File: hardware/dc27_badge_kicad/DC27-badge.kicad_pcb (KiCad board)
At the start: 4 copper layers, 79.1 x 184.5 mm, 141 parts, among them J101 Conn_ARM_JTAG_SWD_10, J102 ShittyAddOnL, J103 ShittyAddOnR, J104 Conn_02x20_Odd_Even, J601 USB_MICRO_RIGHT, Q401 FDN360P, SW108 RESET, SW401 POWER ON, SW801 SKRHAAE010, SW802 SKRHAAE010, U100 BMD-340-A-R-DC27-peripheral-c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, U301 IS31FL3736-QFLS4-TR, U401 MCP73833, U402 LM1117-3.3, U501 CS4344-CZZ, U502 LM4880, U601 CP2102N-A01-GQFN28, U602 TPD3E001DRLR, Y101 32.768Khz XTAL

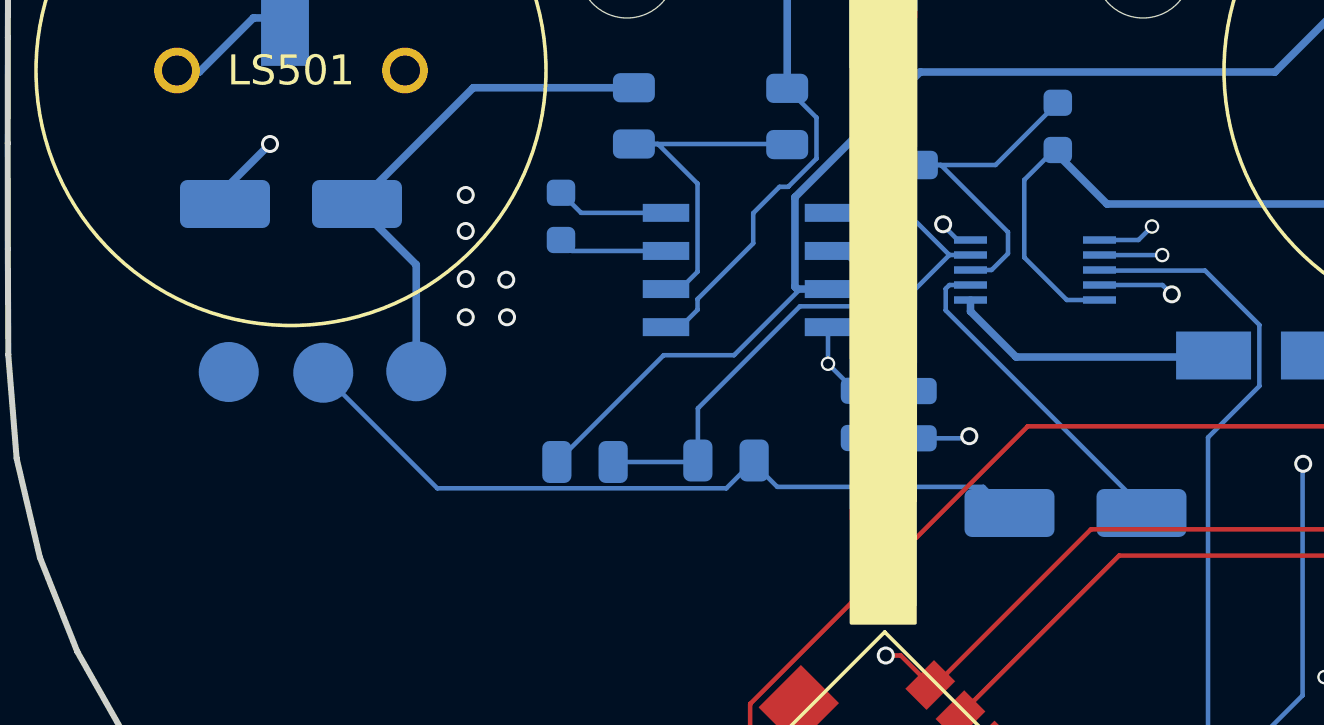
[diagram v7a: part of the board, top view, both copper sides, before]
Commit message: update schematic and pcb with proper audio cap polarity
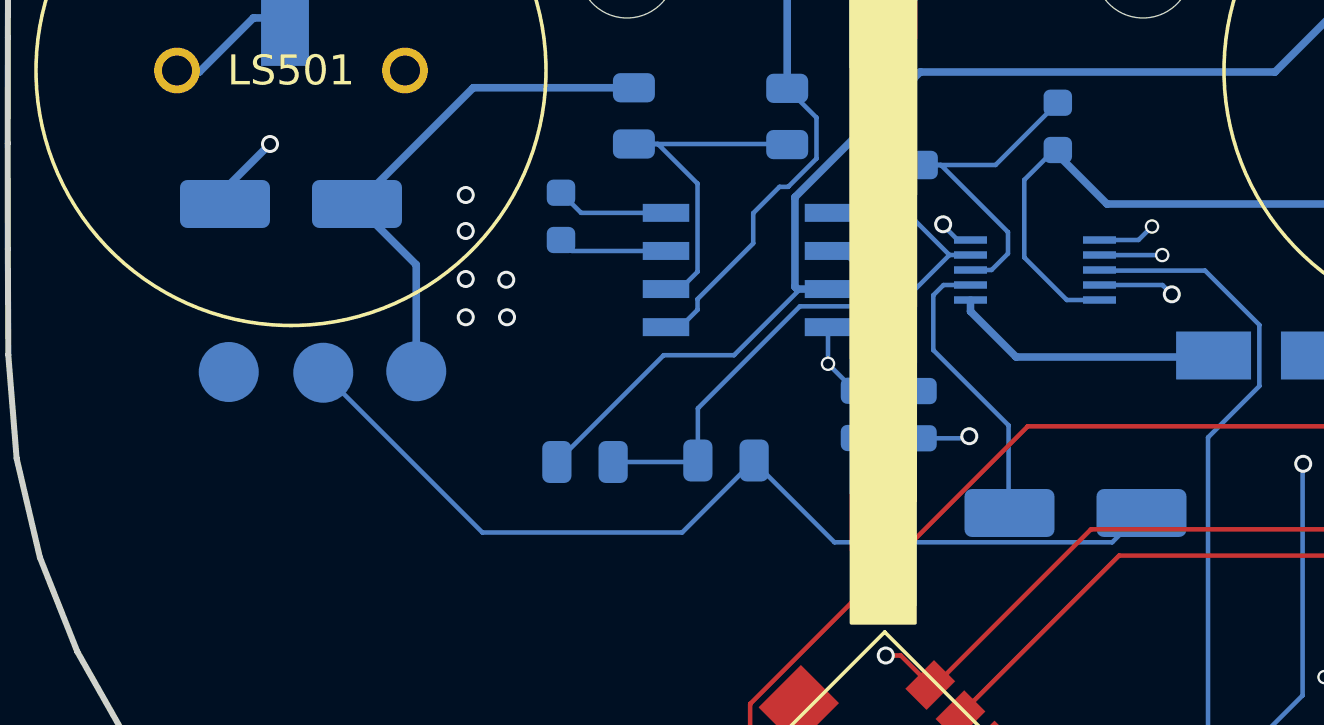
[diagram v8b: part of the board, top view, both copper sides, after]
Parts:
- turned C504 to 0 degrees
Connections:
- R502 pad 2: Net-(C504-Pad1) -> Net-(C504-Pad2)
- R503 pad 2: Net-(C506-Pad1) -> Net-(C506-Pad2)
- TP501 pad 1: Net-(C504-Pad1) -> Net-(C504-Pad2)
- TP502 pad 1: Net-(C506-Pad1) -> Net-(C506-Pad2)
- U501 pad 10: Net-(C504-Pad2) -> Net-(C504-Pad1)
- U501 pad 7: Net-(C506-Pad2) -> Net-(C506-Pad1)
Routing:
- net Net-(C506-Pad2): track 10.6 -> 32.0 mm
- net Net-(C506-Pad1): track 25.7 -> 9.58 mm
- net Net-(C504-Pad2): track 27.7 -> 17.0 mm, vias 2 -> 0
- net Net-(C504-Pad1): track 17.0 -> 27.7 mm, vias 0 -> 2
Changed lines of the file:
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@@
     (thickness 1.6)
     (drawings 191)
-    (tracks 2599)
+    (tracks 2601)
     (zones 0)
     (modules 141)
@@
     )
     (pad 1 smd circle (at 0 0) (size 2 2) (layers B.Cu B.Mask)
-      (net 61 "Net-(C506-Pad1)"))
+      (net 90 "Net-(C506-Pad2)"))
   )
   (module TestPoint:TestPoint_Pad_D2.0mm (layer B.Cu)
@@
     )
     (pad 1 smd circle (at 0 0) (size 2 2) (layers B.Cu B.Mask)
-      (net 53 "Net-(C504-Pad1)"))
+      (net 91 "Net-(C504-Pad2)"))
   )
   (module Diode_SMD:D_0805_2012Metric (layer F.Cu)
@@
   )
   (module Capacitor_SMD:CP_Elec_5x5.3 (layer B.Cu)
-    (at 85.4 53.2 180)
+    (at 85.4 53.2)
     (descr "SMD capacitor, aluminum electrolytic, Nichicon, 5.0x5.3mm")
     (tags "capacitor electrolytic")
     (attr smd)
-    (fp_text reference C504 (at 0 3.7 180) (layer B.SilkS)
+    (fp_text reference C504 (at 0 3.7) (layer B.SilkS)
       (effects (font (size 1 1) (thickness 0.15)) (justify mirror))
     )
-    (fp_text value 3.3uF (at 0 -3.7 180) (layer B.Fab)
+    (fp_text value 3.3uF (at 0 -3.7) (layer B.Fab)
       (effects (font (size 1 1) (thickness 0.15)) (justify mirror))
     )
-    (fp_text user %R (at 0 0 180) (layer B.Fab)
+    (fp_text user %R (at 0 0) (layer B.Fab)
       (effects (font (size 1 1) (thickness 0.15)) (justify mirror))
     )
@@
     (fp_line (start 2.65 2.65) (end 2.65 -2.65) (layer B.Fab) (width 0.1))
     (fp_circle (center 0 0) (end 2.5 0) (layer B.Fab) (width 0.1))
-    (pad 2 smd roundrect (at 2.2 0 180) (size 3 1.6) (layers B.Cu B.Paste B.Mask) (roundrect_rratio 0.15625)
+    (pad 2 smd roundrect (at 2.2 0) (size 3 1.6) (layers B.Cu B.Paste B.Mask) (roundrect_rratio 0.15625)
       (net 91 "Net-(C504-Pad2)"))
-    (pad 1 smd roundrect (at -2.2 0 180) (size 3 1.6) (layers B.Cu B.Paste B.Mask) (roundrect_rratio 0.15625)
+    (pad 1 smd roundrect (at -2.2 0) (size 3 1.6) (layers B.Cu B.Paste B.Mask) (roundrect_rratio 0.15625)
       (net 53 "Net-(C504-Pad1)"))
     (model ${KISYS3DMOD}/Capacitor_SMD.3dshapes/CP_Elec_5x5.3.wrl
@@
     (fp_line (start -1 -0.6) (end -1 0.6) (layer B.Fab) (width 0.1))
     (pad 2 smd roundrect (at 0.9375 0 90) (size 0.975 1.4) (layers B.Cu B.Paste B.Mask) (roundrect_rratio 0.25)
-      (net 53 "Net-(C504-Pad1)"))
+      (net 91 "Net-(C504-Pad2)"))
     (pad 1 smd roundrect (at -0.9375 0 90) (size 0.975 1.4) (layers B.Cu B.Paste B.Mask) (roundrect_rratio 0.25)
       (net 52 "Net-(R501-Pad2)"))
@@
     (fp_line (start -1 -0.6) (end -1 0.6) (layer B.Fab) (width 0.1))
     (pad 2 smd roundrect (at 0.9375 0) (size 0.975 1.4) (layers B.Cu B.Paste B.Mask) (roundrect_rratio 0.25)
-      (net 61 "Net-(C506-Pad1)"))
+      (net 90 "Net-(C506-Pad2)"))
     (pad 1 smd roundrect (at -0.9375 0) (size 0.975 1.4) (layers B.Cu B.Paste B.Mask) (roundrect_rratio 0.25)
       (net 62 "Net-(R503-Pad1)"))
@@
       (net 89 "Net-(C509-Pad1)"))
     (pad 7 smd rect (at 2.15 -0.5 180) (size 1.1 0.25) (layers B.Cu B.Paste B.Mask)
-      (net 90 "Net-(C506-Pad2)"))
+      (net 61 "Net-(C506-Pad1)"))
     (pad 8 smd rect (at 2.15 0 180) (size 1.1 0.25) (layers B.Cu B.Paste B.Mask)
       (net 138 GND))
@@
       (net 1 AVCC))
     (pad 10 smd rect (at 2.15 1 180) (size 1.1 0.25) (layers B.Cu B.Paste B.Mask)
-      (net 91 "Net-(C504-Pad2)"))
+      (net 53 "Net-(C504-Pad1)"))
     (model ${KISYS3DMOD}/Package_SO.3dshapes/TSSOP-10_3x3mm_P0.5mm.step
       (at (xyz 0 0 0))
@@
   (segment (start 98.951201 55.458799) (end 98.951201 52.521201) (width 0.1524) (layer B.Cu) (net 52))
   (segment (start 97.63 51.2) (end 96.83 51.2) (width 0.1524) (layer B.Cu) (net 52) (status 20))
-  (segment (start 96.83 49.325) (end 91.475 49.325) (width 0.254) (layer B.Cu) (net 53) (status 10))
-  (segment (start 91.475 49.325) (end 87.8 53) (width 0.254) (layer B.Cu) (net 53) (status 20))
-  (segment (start 89.575 58.775) (end 89.575 55.225) (width 0.254) (layer B.Cu) (net 53) (status 10))
-  (segment (start 89.575 55.225) (end 87.525 53.175) (width 0.254) (layer B.Cu) (net 53) (status 20))
+  (segment (start 96.83 49.325) (end 91.475 49.325) (width 0.254) (layer B.Cu) (net 91) (status 10))
+  (segment (start 91.475 49.325) (end 87.8 53) (width 0.254) (layer B.Cu) (net 91) (status 20))
+  (segment (start 89.575 58.775) (end 89.575 55.225) (width 0.254) (layer B.Cu) (net 91) (status 10))
+  (segment (start 89.575 55.225) (end 87.525 53.175) (width 0.254) (layer B.Cu) (net 91) (status 20))
   (segment (start 96.37 102.625) (end 96.34 102.655) (width 0.1524) (layer F.Cu) (net 54))
   (segment (start 96.37 102.0875) (end 96.37 102.625) (width 0.1524) (layer F.Cu) (net 54) (status 10))
@@
   (segment (start 115.940357 203.575357) (end 115.940357 205.629643) (width 0.152) (layer F.Cu) (net 60))
   (segment (start 115.940357 205.629643) (end 114.86 206.71) (width 0.152) (layer F.Cu) (net 60) (status 20))
-  (segment (start 100.75 61.6625) (end 100.8375 61.75) (width 0.1524) (layer B.Cu) (net 61) (status 30))
-  (segment (start 108.47929 62.62929) (end 101.60929 62.62929) (width 0.1524) (layer B.Cu) (net 61))
-  (segment (start 109.35 63.5) (end 108.47929 62.62929) (width 0.1524) (layer B.Cu) (net 61) (status 10))
-  (segment (start 101.60929 62.62929) (end 100.82 61.84) (width 0.1524) (layer B.Cu) (net 61) (status 20))
-  (segment (start 99.91129 62.67621) (end 90.27621 62.67621) (width 0.1524) (layer B.Cu) (net 61))
-  (segment (start 100.8375 61.75) (end 99.91129 62.67621) (width 0.1524) (layer B.Cu) (net 61) (status 10))
-  (segment (start 90.27621 62.67621) (end 86.475 58.875) (width 0.1524) (layer B.Cu) (net 61) (status 20))
+  (segment (start 100.75 61.6625) (end 100.8375 61.75) (width 0.1524) (layer B.Cu) (net 90) (status 30))
   (segment (start 98.9125 61.8) (end 98.9625 61.75) (width 0.1524) (layer B.Cu) (net 62) (status 30))
   (segment (start 96.1375 61.8) (end 98.9125 61.8) (width 0.1524) (layer B.Cu) (net 62) (status 30))
@@
   (segment (start 108.05 56.4) (end 108.05 56.779) (width 0.254) (layer B.Cu) (net 89) (status 10))
   (segment (start 109.571 58.3) (end 116.2 58.3) (width 0.254) (layer B.Cu) (net 89) (status 20))
-  (segment (start 107.3476 55.9) (end 107.223799 56.023801) (width 0.1524) (layer B.Cu) (net 90))
-  (segment (start 107.223799 56.745961) (end 113.597838 63.12) (width 0.1524) (layer B.Cu) (net 90) (status 20))
-  (segment (start 107.223799 56.023801) (end 107.223799 56.745961) (width 0.1524) (layer B.Cu) (net 90))
-  (segment (start 108.05 55.9) (end 107.3476 55.9) (width 0.1524) (layer B.Cu) (net 90) (status 10))
-  (segment (start 108.05 54.4) (end 107.625 54.4) (width 0.1524) (layer B.Cu) (net 91) (status 30))
-  (via (at 107.138421 53.875937) (size 0.6) (drill 0.4) (layers F.Cu B.Cu) (net 91))
-  (segment (start 107.138421 53.913421) (end 107.138421 53.875937) (width 0.1524) (layer B.Cu) (net 91))
-  (segment (start 107.625 54.4) (end 107.138421 53.913421) (width 0.1524) (layer B.Cu) (net 91) (status 10))
-  (via (at 84.7 51.2) (size 0.6) (drill 0.4) (layers F.Cu B.Cu) (net 91))
-  (segment (start 104.462484 51.2) (end 84.7 51.2) (width 0.254) (layer PWR) (net 91))
-  (segment (start 107.138421 53.875937) (end 104.462484 51.2) (width 0.254) (layer PWR) (net 91))
-  (segment (start 84.7 51.2) (end 82.6 53.3) (width 0.254) (layer B.Cu) (net 91) (status 20))
+  (segment (start 108.05 54.4) (end 107.625 54.4) (width 0.1524) (layer B.Cu) (net 53) (status 30))
+  (via (at 107.138421 53.875937) (size 0.6) (drill 0.4) (layers F.Cu B.Cu) (net 53))
+  (segment (start 107.138421 53.913421) (end 107.138421 53.875937) (width 0.1524) (layer B.Cu) (net 53))
+  (segment (start 107.625 54.4) (end 107.138421 53.913421) (width 0.1524) (layer B.Cu) (net 53) (status 10))
+  (via (at 84.7 51.2) (size 0.6) (drill 0.4) (layers F.Cu B.Cu) (net 53))
+  (segment (start 104.462484 51.2) (end 84.7 51.2) (width 0.254) (layer PWR) (net 53))
+  (segment (start 107.138421 53.875937) (end 104.462484 51.2) (width 0.254) (layer PWR) (net 53))
+  (segment (start 84.7 51.2) (end 82.6 53.3) (width 0.254) (layer B.Cu) (net 53) (status 20))
+  (segment (start 108.05 55.9) (end 107.625 55.9) (width 0.152) (layer B.Cu) (net 61))
+  (segment (start 107.625 55.9) (end 107.15 55.9) (width 0.152) (layer B.Cu) (net 61))
+  (segment (start 107.15 55.9) (end 106.81 56.24) (width 0.152) (layer B.Cu) (net 61))
+  (segment (start 106.81 56.24) (end 106.81 58.07) (width 0.152) (layer B.Cu) (net 61))
+  (segment (start 106.81 58.07) (end 109.32 60.58) (width 0.152) (layer B.Cu) (net 61))
+  (segment (start 109.32 60.58) (end 109.32 63.4) (width 0.152) (layer B.Cu) (net 61))
+  (segment (start 98.4375 64.15) (end 91.78 64.15) (width 0.152) (layer B.Cu) (net 90))
+  (segment (start 100.8375 61.75) (end 98.4375 64.15) (width 0.152) (layer B.Cu) (net 90))
+  (segment (start 91.78 64.15) (end 86.48 58.85) (width 0.152) (layer B.Cu) (net 90))
+  (segment (start 112.77399 64.47601) (end 103.51601 64.47601) (width 0.152) (layer B.Cu) (net 90))
+  (segment (start 113.75 63.5) (end 112.77399 64.47601) (width 0.152) (layer B.Cu) (net 90))
+  (segment (start 103.51601 64.47601) (end 100.89 61.85) (width 0.152) (layer B.Cu) (net 90))
   (segment (start 81.6 49.2) (end 81.4 49) (width 0.381) (layer F.Cu) (net 92) (status 30))
   (segment (start 84.14717 46.99748) (end 82.34465 48.8) (width 0.254) (layer B.Cu) (net 92) (status 20))
